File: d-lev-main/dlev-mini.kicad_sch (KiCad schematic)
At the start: 41 parts, among them J1 S12B-PH-SM4-TB, J3 S8B-PH-SM4-TB, J4 S8B-PH-SM4-TB, J5 S6B-PH-SM4-TB, Q2 BSS138, Q3 BSS138, Q4 BSS138, Q5 BSS138, U4 AMS1117-3.3

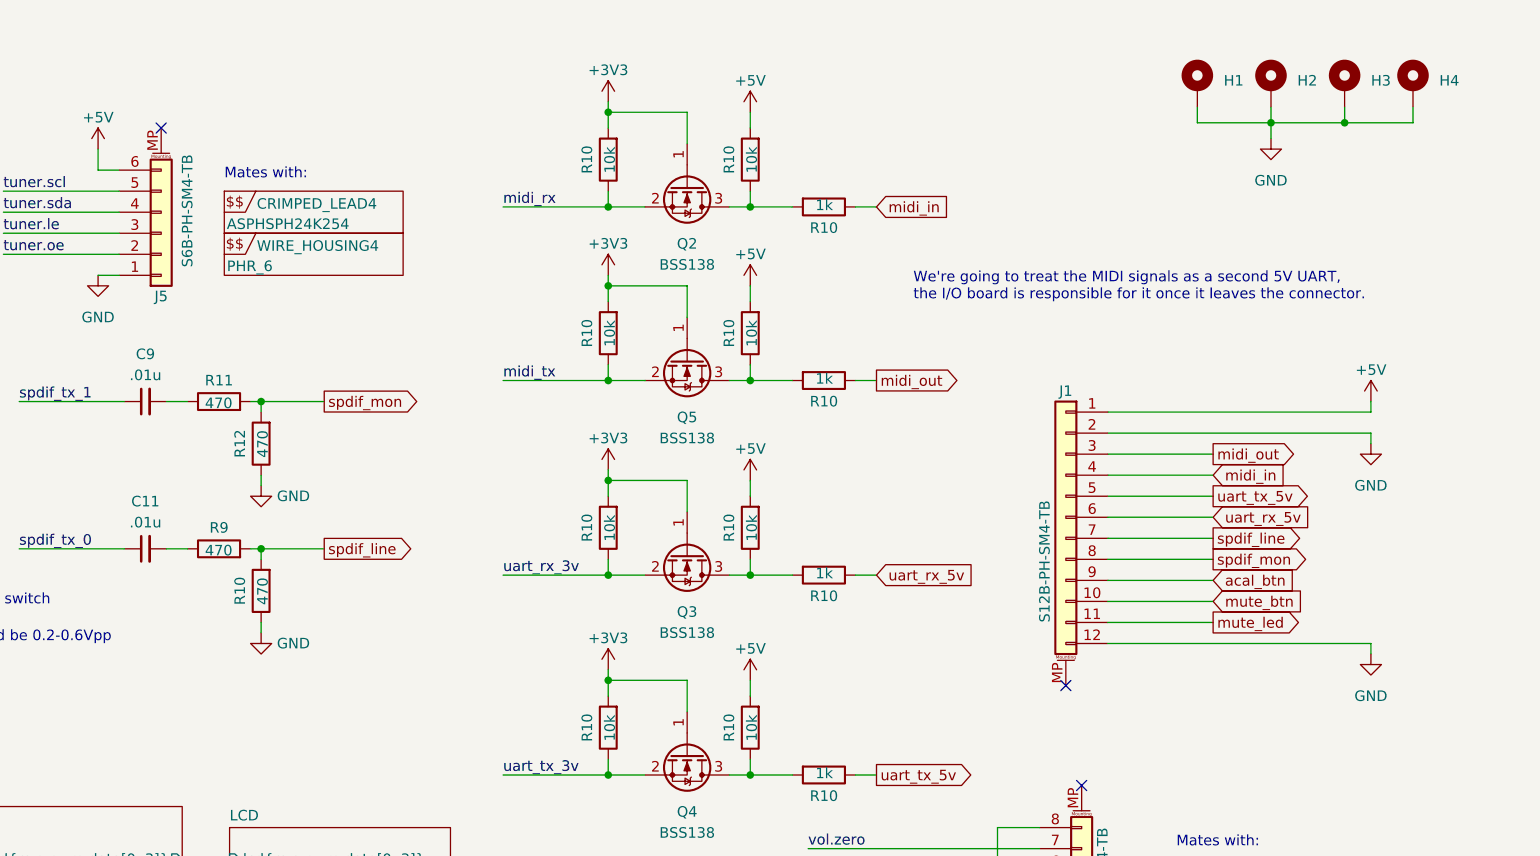
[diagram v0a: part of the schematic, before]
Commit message: Improve routing and rearrange I/O connector
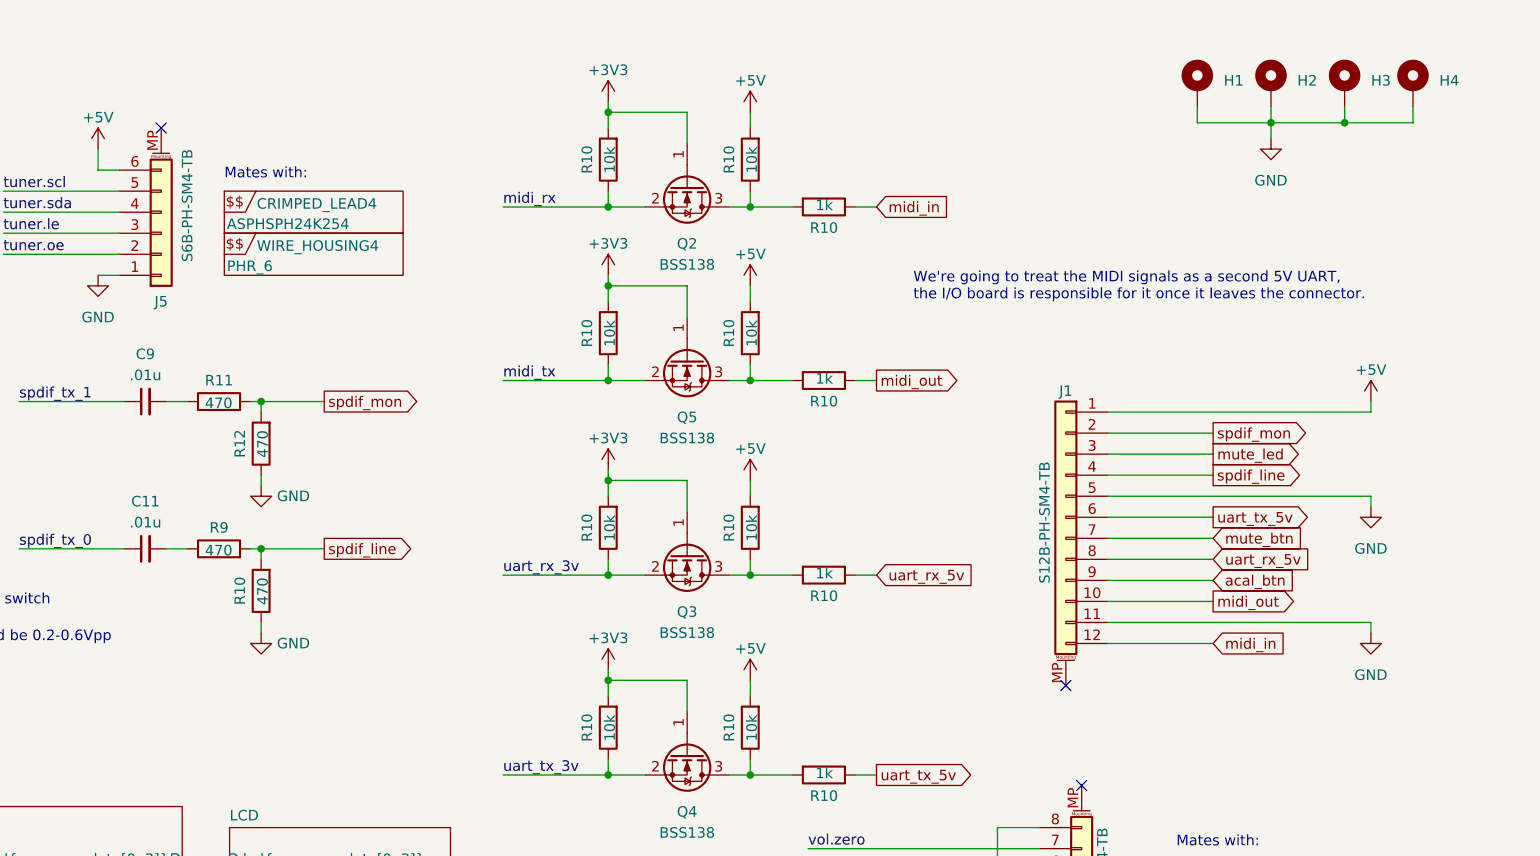
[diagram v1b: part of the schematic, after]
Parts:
- J1: symbol Connector_Generic_MountingPin:Conn_01x12_MountingPin -> assorted:Conn_01x12_MountingPin
- J3, J4: symbol Connector_Generic_MountingPin:Conn_01x08_MountingPin -> assorted:Conn_01x08_MountingPin
- J5: symbol Connector_Generic_MountingPin:Conn_01x06_MountingPin -> assorted:Conn_01x06_MountingPin
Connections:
- net GND: now also J1.11 (Pin_11), J1.5 (Pin_5); no longer J1.12 (Pin_12), J1.2 (Pin_2)
- net midi_in: now also J1.12 (Pin_12); no longer J1.4 (Pin_4)
- net midi_out: now also J1.10 (Pin_10); no longer J1.3 (Pin_3)
- net mute_btn: now also J1.7 (Pin_7); no longer J1.10 (Pin_10)
- net mute_led: now also J1.3 (Pin_3); no longer J1.11 (Pin_11)
- net spdif_line: now also J1.4 (Pin_4); no longer J1.7 (Pin_7)
- net spdif_mon: now also J1.2 (Pin_2); no longer J1.8 (Pin_8)
- net uart_rx_5v: now also J1.8 (Pin_8); no longer J1.6 (Pin_6)
- net uart_tx_5v: now also J1.6 (Pin_6); no longer J1.5 (Pin_5)
- net at J3.MP (MountPin): now also J3.9 (MountPin2)
- net at J4.MP (MountPin): now also J4.9 (MountPin2)

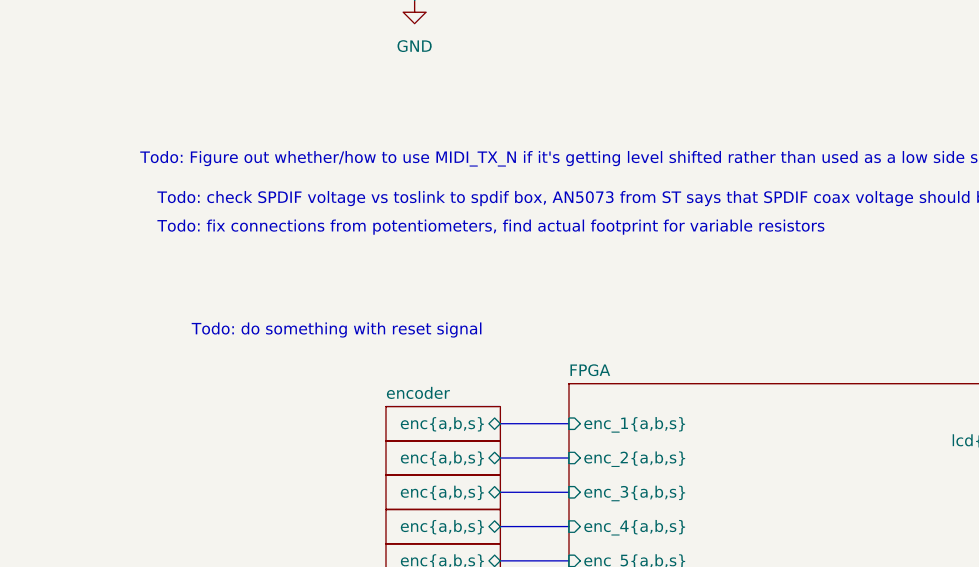
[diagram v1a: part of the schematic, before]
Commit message: Via stitching around afe traces and add fix for lcd contrast pot
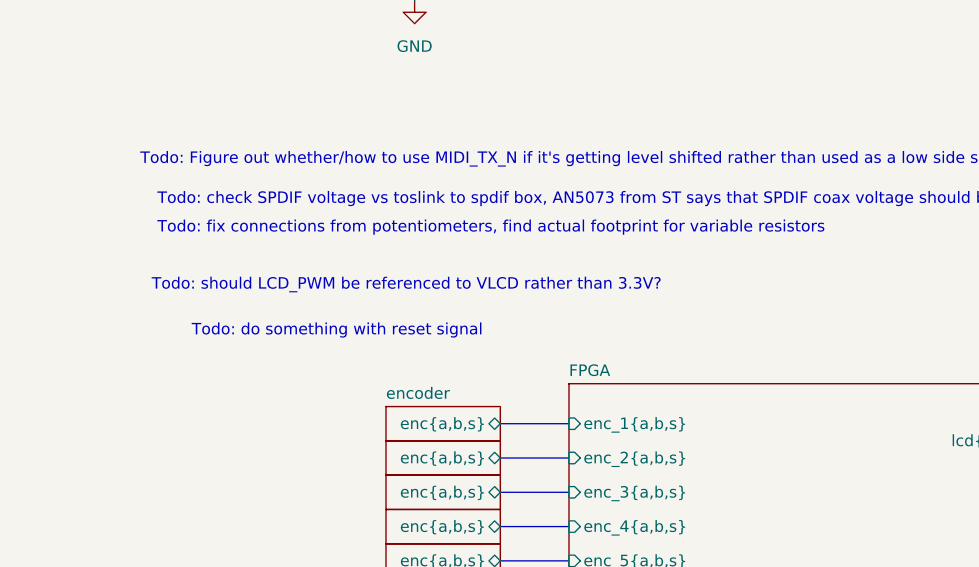
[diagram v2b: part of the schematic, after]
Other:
- note added: "Todo: should LCD_PWM be referenced to VLCD rather than 3.3V?"
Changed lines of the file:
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@@
+    (effects (font (size 1.27 1.27)) (justify left bottom))
+  )
+  (text "Todo: should LCD_PWM be referenced to VLCD rather than 3.3V?"
+    (at 17.145 93.345 0)
     (effects (font (size 1.27 1.27)) (justify left bottom))
   )

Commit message: many many changes'
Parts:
- removed Q2, Q3, Q4, Q5: BSS138, Package_TO_SOT_SMD:SOT-23, symbol Transistor_FET:BSS138
- removed R10 (x4): 1k, Resistor_SMD:R_0603_1608Metric, symbol Device:R
- removed R10 (x8): 10k, Resistor_SMD:R_0603_1608Metric, symbol Device:R
- added TP3: GND, TestPoint:TestPoint_Pad_D1.0mm, symbol Connector:TestPoint
- added TP3: VDD, TestPoint:TestPoint_Pad_D1.0mm, symbol Connector:TestPoint
- R10: now not fitted
- renumbered J5 to J1, J1 to J3, J3 to J4, J4 to J5
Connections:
- net GND: now also TP3.1
- net +5V renamed VDD
- net VDD: now also TP3.1
- net uart_rx_5v renamed uart_rx
- net uart_tx_5v renamed uart_tx
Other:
- note added: "Todo: use internal pull ups on ACAL_BTN and MUTE_BTN (no reason to risk pulling them up to 3v3 from other regulator)"

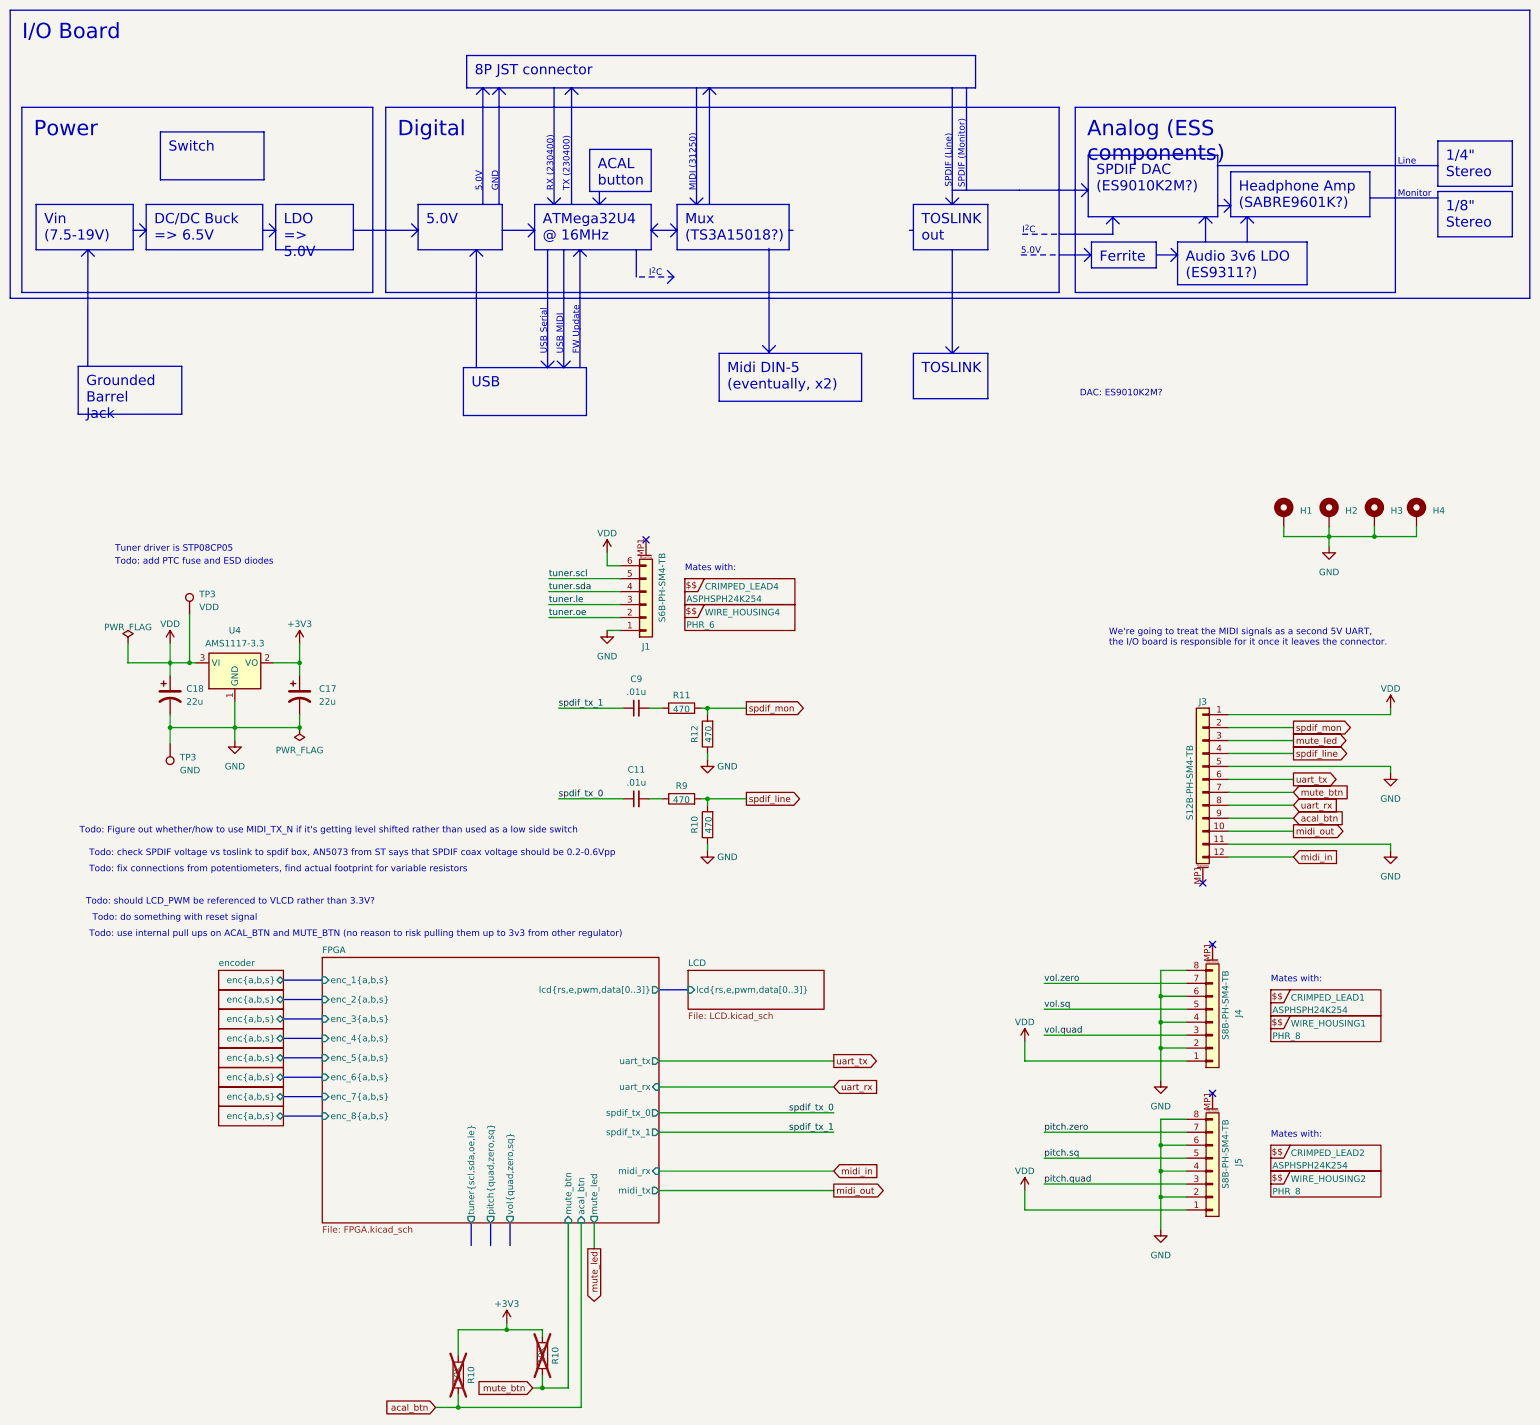
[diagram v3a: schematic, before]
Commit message: round tracks and teardrops
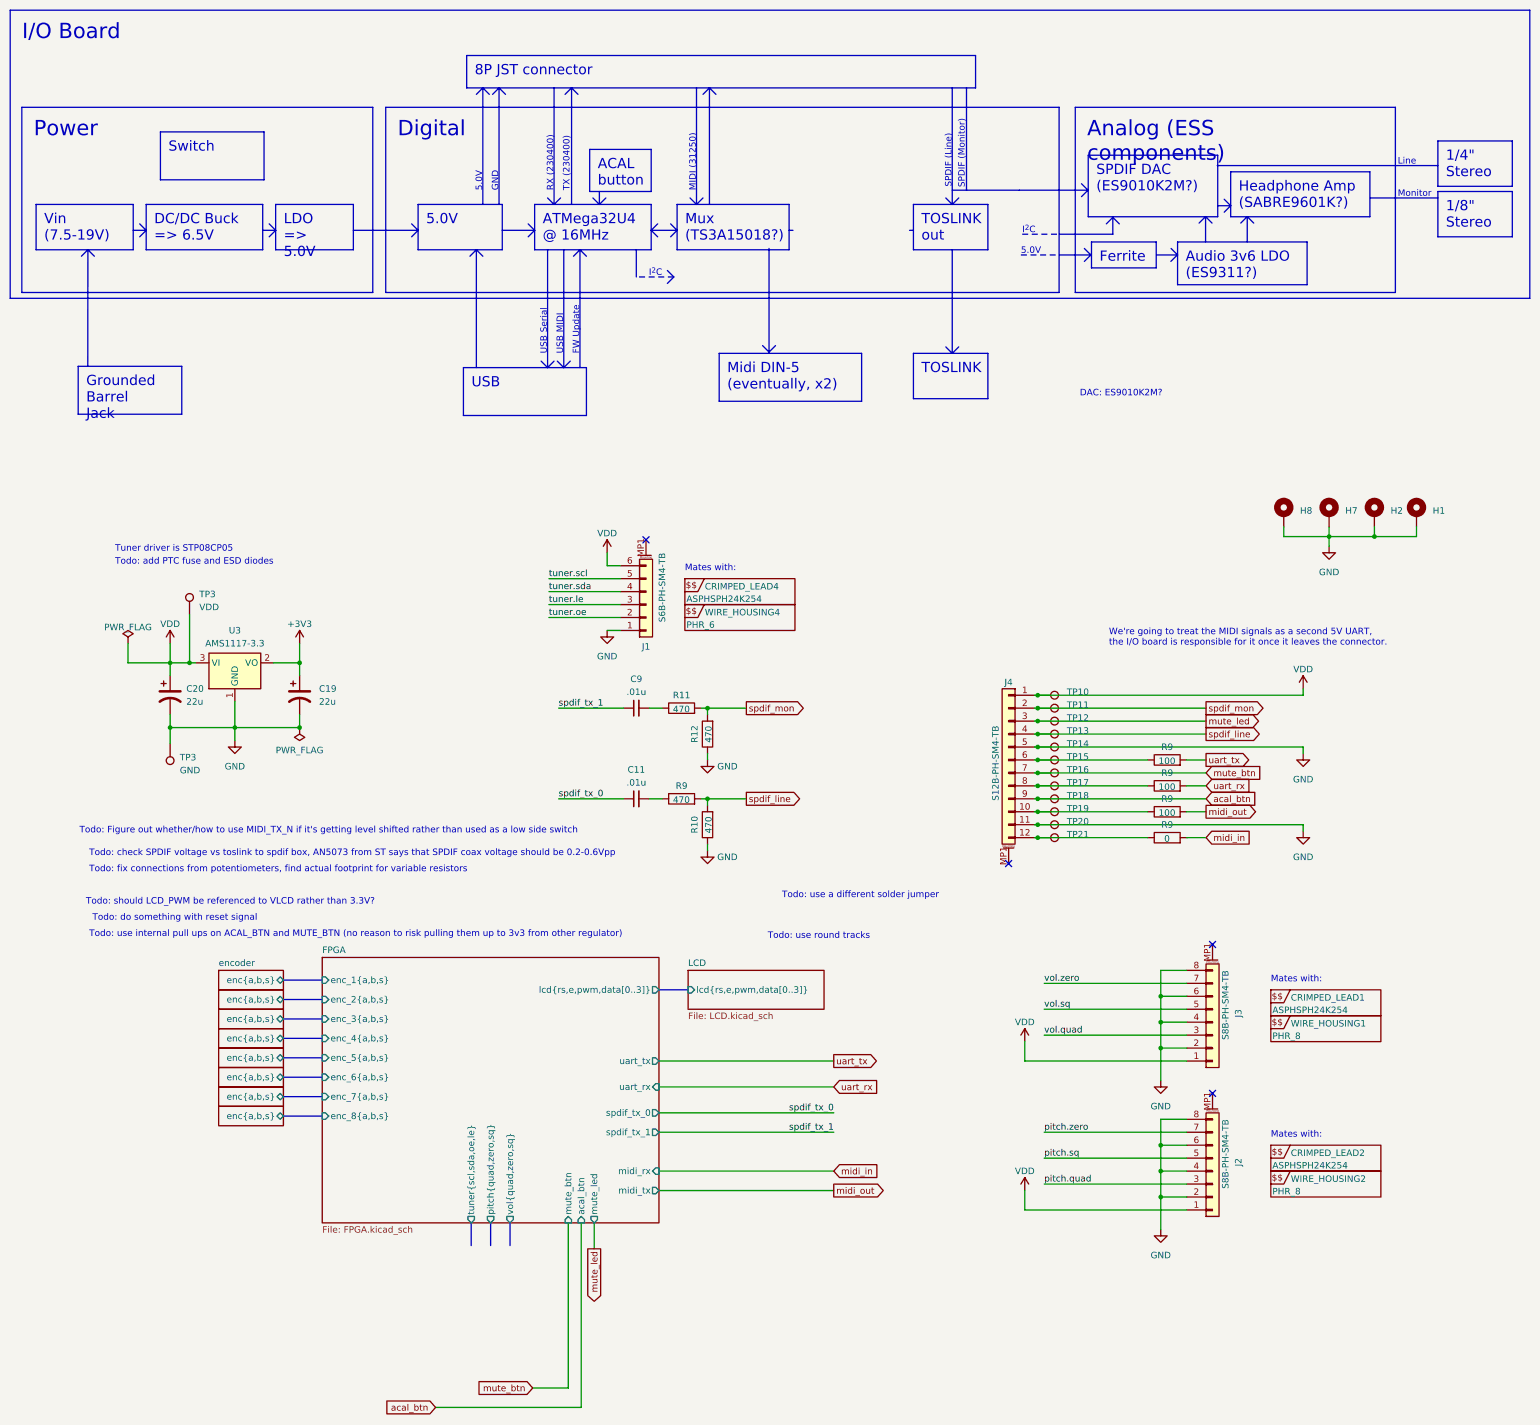
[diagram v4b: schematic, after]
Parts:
- removed R10 (x2): 10k, Resistor_SMD:R_0603_1608Metric, symbol Device:R
- added R9: 0, Resistor_SMD:R_0603_1608Metric, symbol Device:R
- added R9 (x3): 100, Resistor_SMD:R_0603_1608Metric, symbol Device:R
- added TP10, TP11, TP12, TP13, TP14, TP15, TP16, TP17, TP18, TP19, TP20, TP21: TestPoint, TestPoint:TestPoint_Pad_D1.0mm, symbol Connector:TestPoint
- renumbered C17 to C19, C18 to C20, H4 to H1, H3 to H2, H2 to H7, H1 to H8, J5 to J2, J4 to J3, J3 to J4, U4 to U3
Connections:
- net GND: now also TP14.1, TP20.1
- net VDD: now also TP10.1
- net acal_btn: now also TP18.1
- net midi_in: now also R9.2; no longer J4.12 (Pin_12)
- net midi_out: now also R9.2; no longer J4.10 (Pin_10)
- net mute_btn: now also TP16.1
- net mute_led: now also TP12.1
- net spdif_line: now also TP13.1
- net spdif_mon: now also TP11.1
- net uart_rx: now also R9.2; no longer J4.8 (Pin_8)
- net uart_tx: now also R9.2; no longer J4.6 (Pin_6)
- new net: J4.12 (Pin_12), R9.1, TP21.1
- new net: J4.8 (Pin_8), R9.1, TP17.1
- new net: J4.10 (Pin_10), R9.1, TP19.1
- new net: J4.6 (Pin_6), R9.1, TP15.1
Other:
- note added: "Todo: use a different solder jumper"
- note added: "Todo: use round tracks"
- moved on the sheet: J4

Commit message: many board updates
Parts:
- added R9 (x2): 100, Resistor_SMD:R_0603_1608Metric, symbol Device:R
- C11, C9: value .01u -> 100n
- R10, R12: value 470 -> 110
- R11, R9: value 470 -> 210
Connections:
- net acal_btn: now also R9.2; no longer J4.9 (Pin_9), TP18.1
- net mute_btn: now also R9.2; no longer J4.7 (Pin_7), TP16.1
- net spdif_line: now also C11.2; no longer R10.2, R9.2
- net spdif_mon: now also C9.2; no longer R11.2, R12.2
- net spdif_tx_0: now also R9.1; no longer C11.1
- net spdif_tx_1: now also R11.1; no longer C9.1
- new net: J4.9 (Pin_9), R9.1, TP18.1
- new net: J4.7 (Pin_7), R9.1, TP16.1
- new net: C9.1, R11.2, R12.2
- new net: C11.1, R10.2, R9.2
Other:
- moved on the sheet: C11, C9, R11, R9
